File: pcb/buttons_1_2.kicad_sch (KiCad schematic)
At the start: 38 parts

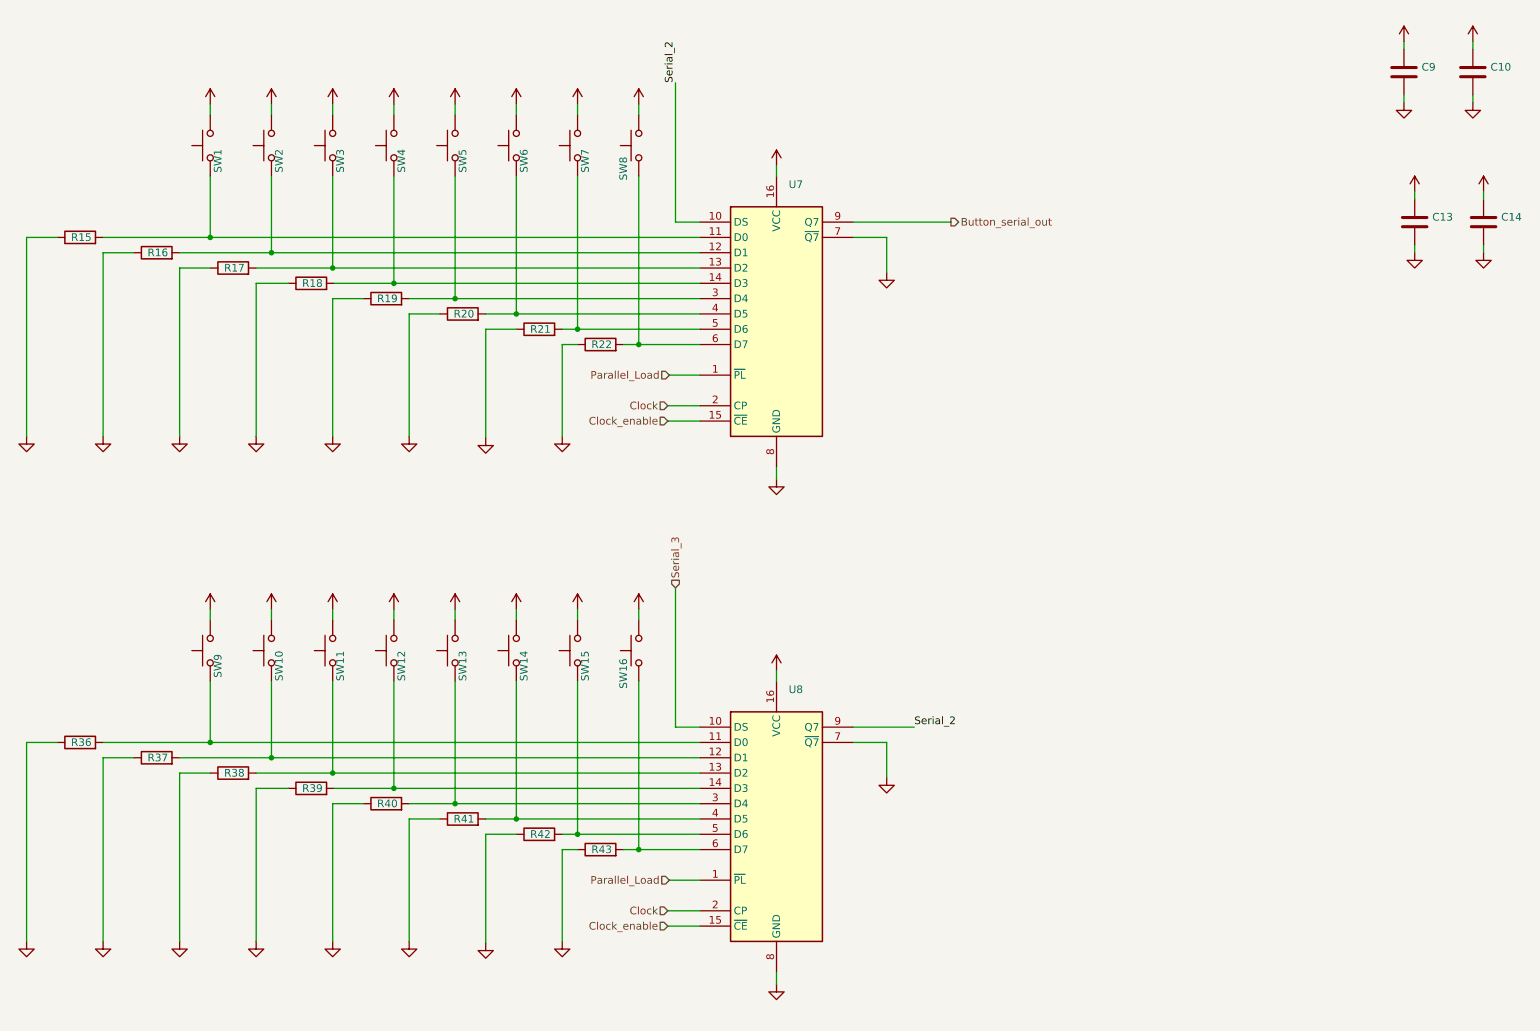
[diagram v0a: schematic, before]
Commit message: reassigned designators and layout progress
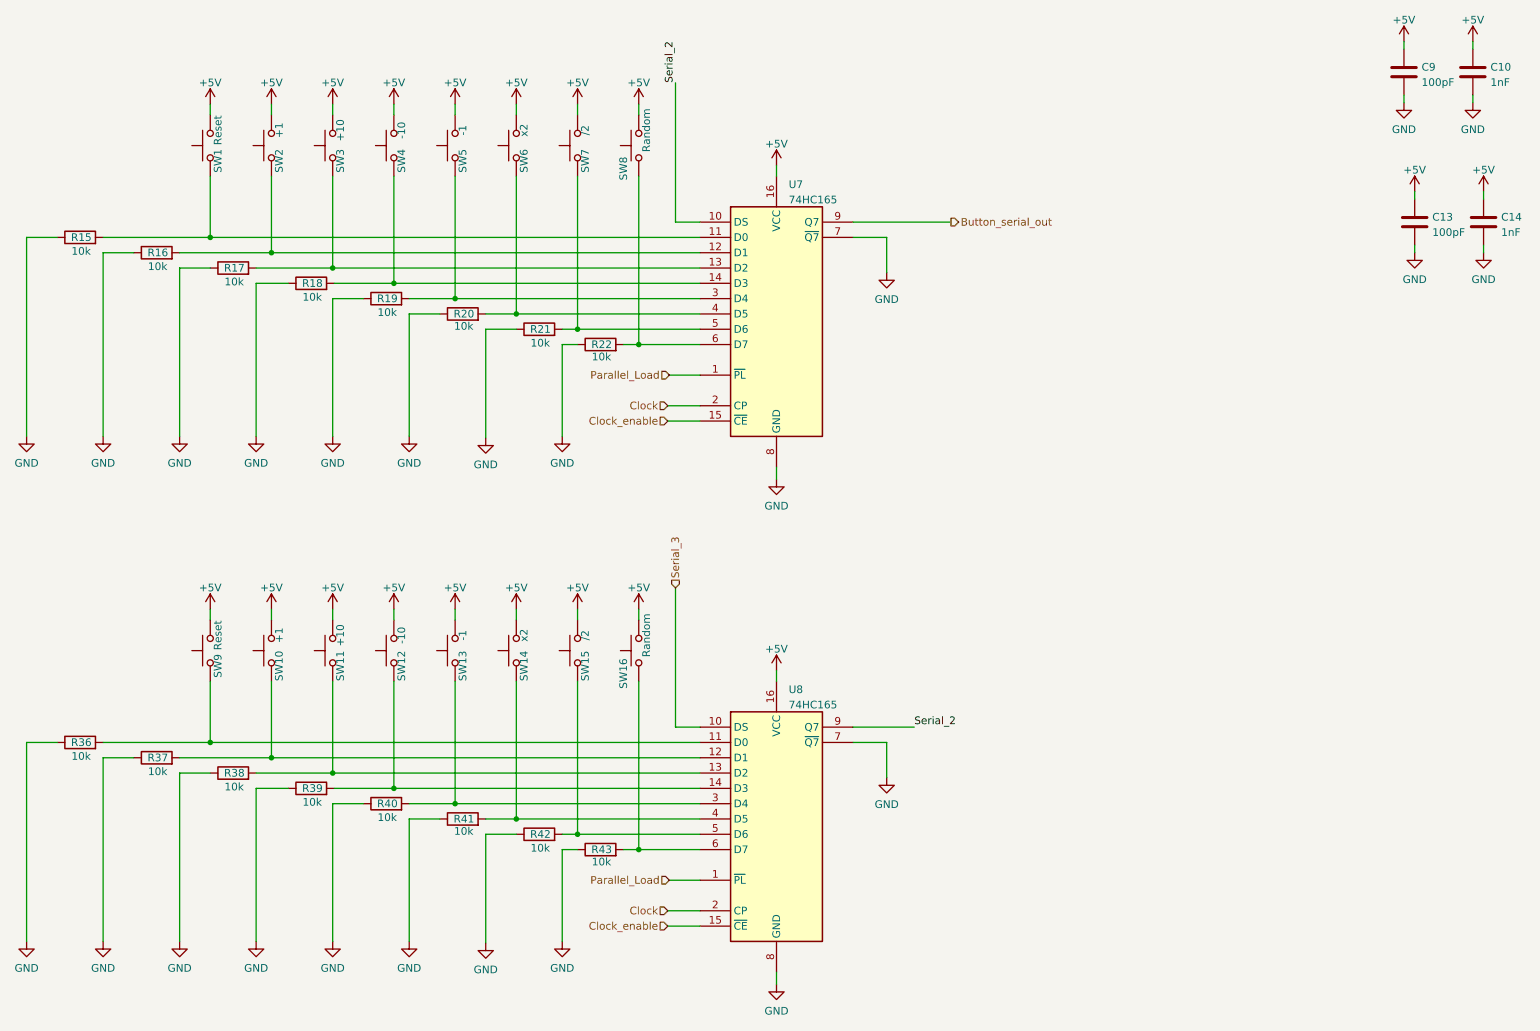
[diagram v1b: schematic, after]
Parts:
- C10, C14: value (none) -> 1nF; footprint (none) -> Capacitor_THT:C_Disc_D3.8mm_W2.6mm_P2.50mm
- C13, C9: value (none) -> 100pF; footprint (none) -> Capacitor_THT:C_Disc_D3.8mm_W2.6mm_P2.50mm
- R15, R16, R17, R18, R19, R20, R21, R22, R36, R37, R38, R39, R40, R41, R42, R43: value (none) -> 10k; footprint (none) -> Resistor_THT:R_Axial_DIN0207_L6.3mm_D2.5mm_P7.62mm_Horizontal
- SW1, SW9: value (none) -> Reset; footprint (none) -> Button_Switch_THT:SW_PUSH_6mm_H5mm
- SW10, SW2: value (none) -> +1; footprint (none) -> Button_Switch_THT:SW_PUSH_6mm_H5mm
- SW11, SW3: value (none) -> +10; footprint (none) -> Button_Switch_THT:SW_PUSH_6mm_H5mm
- SW12, SW4: value (none) -> -10; footprint (none) -> Button_Switch_THT:SW_PUSH_6mm_H5mm
- SW13, SW5: value (none) -> -1; footprint (none) -> Button_Switch_THT:SW_PUSH_6mm_H5mm
- SW14, SW6: value (none) -> x2; footprint (none) -> Button_Switch_THT:SW_PUSH_6mm_H5mm
- SW15, SW7: value (none) -> /2; footprint (none) -> Button_Switch_THT:SW_PUSH_6mm_H5mm
- SW16, SW8: value (none) -> Random; footprint (none) -> Button_Switch_THT:SW_PUSH_6mm_H5mm
- U7, U8: value (none) -> 74HC165; footprint (none) -> Package_DIP:DIP-16_W7.62mm_LongPads

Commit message: fewer parts and reduced to prototyping board with more logic analyzer pins
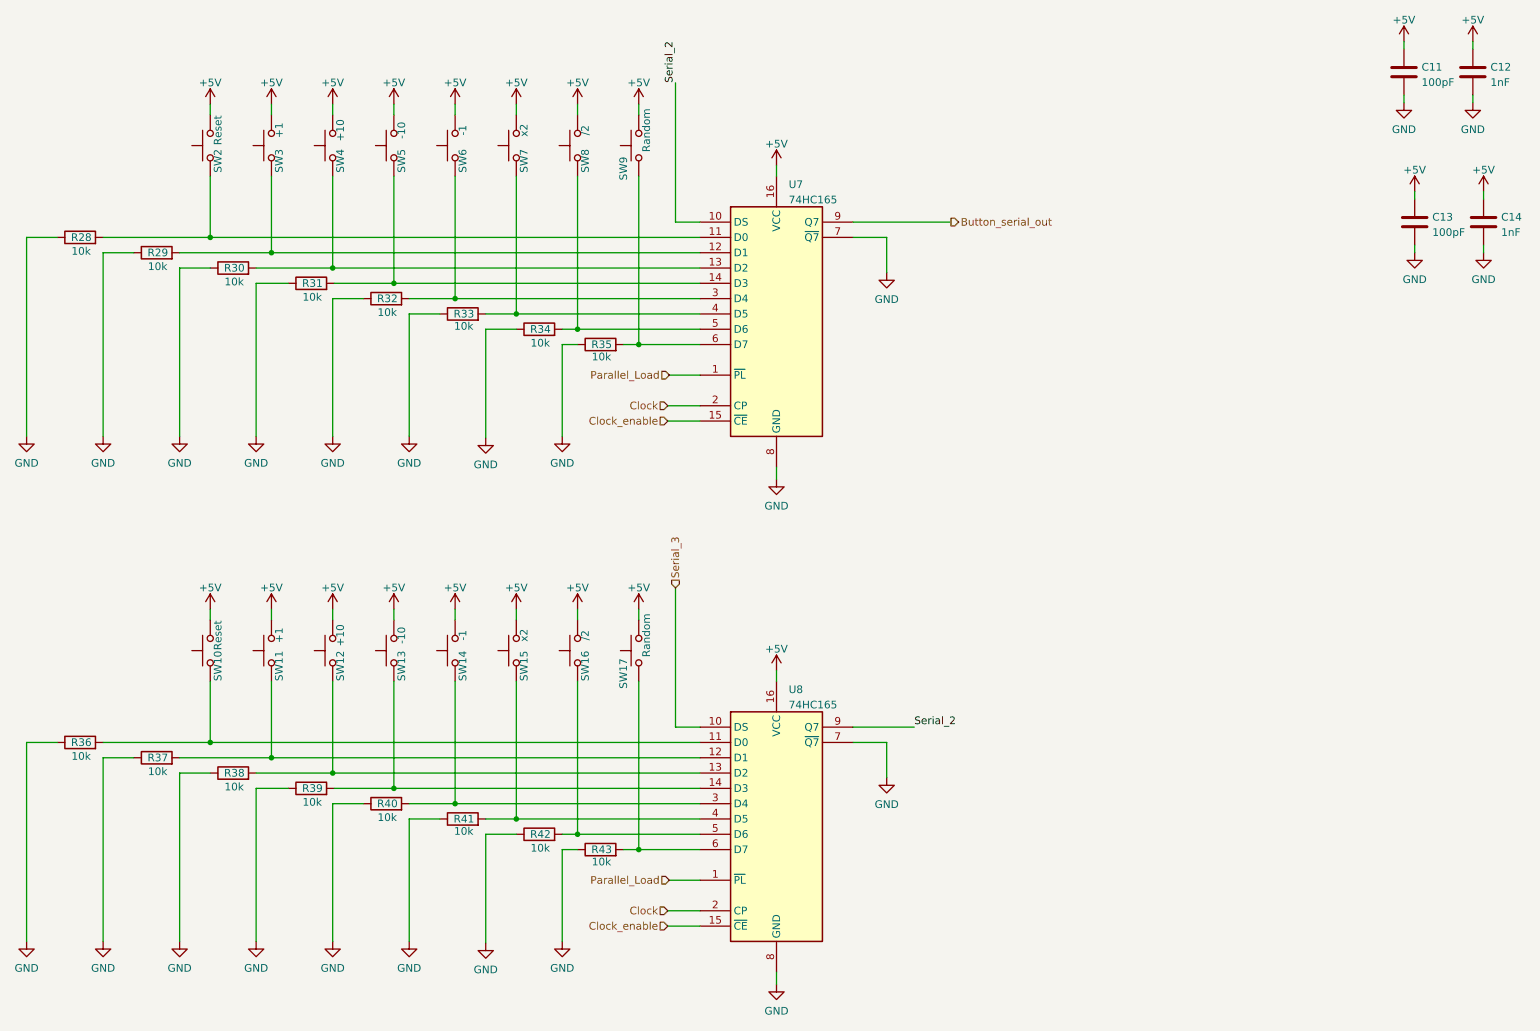
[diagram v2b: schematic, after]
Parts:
- renumbered C9 to C11, C10 to C12, R15 to R28, R16 to R29, R17 to R30, R18 to R31, R19 to R32, R20 to R33, R21 to R34, R22 to R35, SW9 to SW10, SW10 to SW11, SW11 to SW12, SW12 to SW13, SW13 to SW14, SW14 to SW15, SW15 to SW16, SW16 to SW17, SW1 to SW2, SW2 to SW3, SW3 to SW4, SW4 to SW5, SW5 to SW6, SW6 to SW7, SW7 to SW8, SW8 to SW9

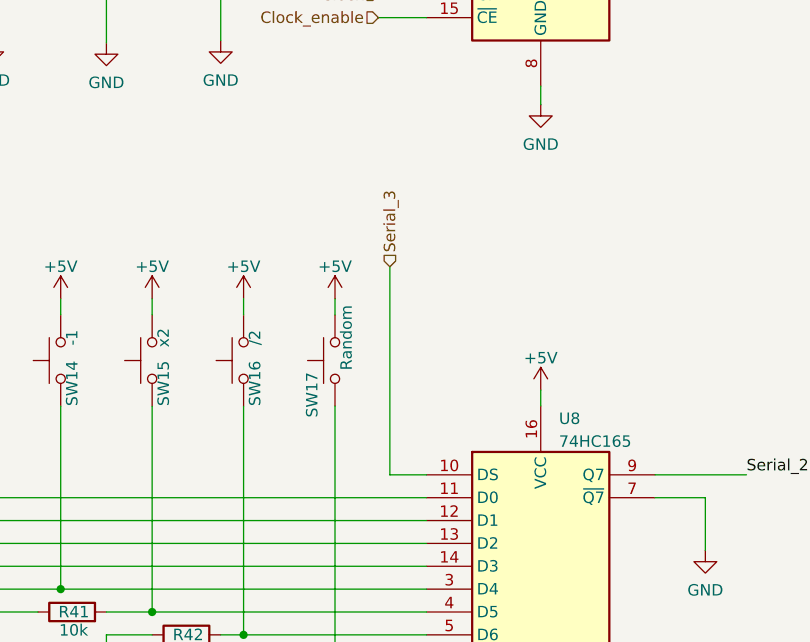
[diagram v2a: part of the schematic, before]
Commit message: reduced to 2 displays and logig analyzer output added
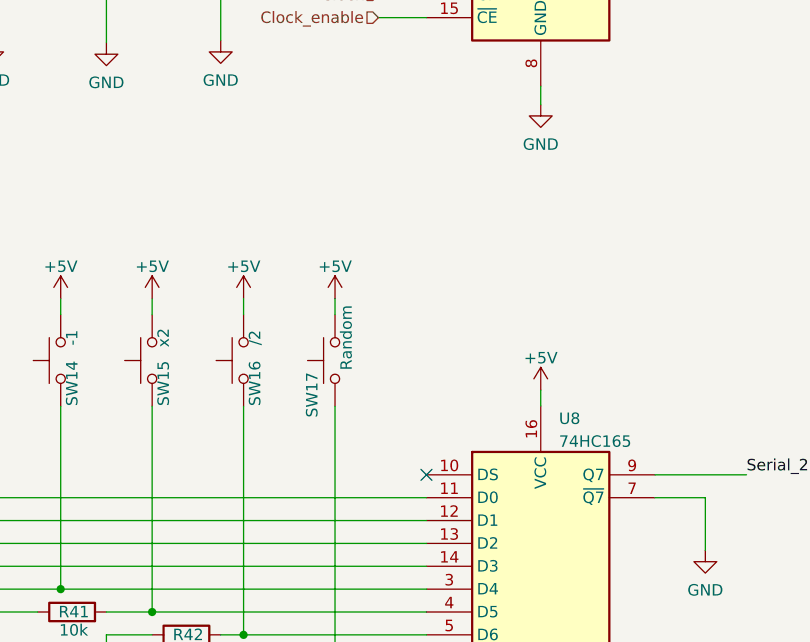
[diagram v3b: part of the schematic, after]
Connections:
- net Serial_3: no longer names the net of U8.10 (DS)
- no-connect marks 0 -> 1
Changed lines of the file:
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@@
   (junction (at 99.06 60.96) (diameter 0) (color 0 0 0 0)
   )
+  (no_connect (at 139.7 132.08))
   (wire (pts (xy 152.4 88.9) (xy 152.4 90.932))
     (stroke (width 0) (type default) (color 0 0 0 0))
@@
     (stroke (width 0) (type default) (color 0 0 0 0))
   )
-  (wire (pts (xy 135.636 108.966) (xy 135.636 132.08))
-    (stroke (width 0) (type default) (color 0 0 0 0))
-  )
   (wire (pts (xy 53.34 139.7) (xy 53.34 167.64))
     (stroke (width 0) (type default) (color 0 0 0 0))
@@
   )
   (wire (pts (xy 66.04 58.42) (xy 66.04 83.82))
-    (stroke (width 0) (type default) (color 0 0 0 0))
-  )
-  (wire (pts (xy 139.7 132.08) (xy 135.636 132.08))
     (stroke (width 0) (type default) (color 0 0 0 0))
   )
@@
     (effects (font (size 1.27 1.27)) (justify right))
   )
-  (hierarchical_label "Serial_3" (shape input) (at 135.636 108.966 90)
-    (effects (font (size 1.27 1.27)) (justify left))
-  )
   (hierarchical_label "Parallel_Load" (shape input) (at 134.62 73.66 180)

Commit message: new parts and stuff
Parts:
- added J12: Conn_01x07_Male, Connector_PinHeader_2.54mm:PinHeader_1x07_P2.54mm_Vertical, symbol Connector:Conn_01x07_Male
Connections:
- net +5V: now also J12.7 (Pin_7)
- net Button_serial_out: now also J12.6 (Pin_6)
- net Clock: now also J12.4 (Pin_4)
- net Clock_enable: now also J12.3 (Pin_3)
- net GND: now also J12.1 (Pin_1)
- net Parallel_Load: now also J12.5 (Pin_5)
- net Serial_2: now also J12.2 (Pin_2)
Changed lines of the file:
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@@
   )
   (no_connect (at 139.7 132.08))
+  (wire (pts (xy 218.44 124.46) (xy 238.76 124.46))
+    (stroke (width 0) (type default) (color 0 0 0 0))
+  )
   (wire (pts (xy 152.4 88.9) (xy 152.4 90.932))
     (stroke (width 0) (type default) (color 0 0 0 0))
@@
     (stroke (width 0) (type default) (color 0 0 0 0))
   )
+  (wire (pts (xy 218.44 115.062) (xy 218.44 116.84))
+    (stroke (width 0) (type default) (color 0 0 0 0))
+  )
   (wire (pts (xy 96.52 147.32) (xy 91.44 147.32))
     (stroke (width 0) (type default) (color 0 0 0 0))
@@
     (stroke (width 0) (type default) (color 0 0 0 0))
   )
+  (wire (pts (xy 218.44 132.08) (xy 218.44 134.112))
+    (stroke (width 0) (type default) (color 0 0 0 0))
+  )
+  (wire (pts (xy 218.44 119.38) (xy 238.76 119.38))
+    (stroke (width 0) (type default) (color 0 0 0 0))
+  )
   (wire (pts (xy 134.366 165.1) (xy 139.7 165.1))
     (stroke (width 0) (type default) (color 0 0 0 0))
   )
+  (wire (pts (xy 218.44 129.54) (xy 238.76 129.54))
+    (stroke (width 0) (type default) (color 0 0 0 0))
+  )
   (wire (pts (xy 129.54 124.46) (xy 129.54 152.4))
     (stroke (width 0) (type default) (color 0 0 0 0))
@@
     (stroke (width 0) (type default) (color 0 0 0 0))
   )
+  (wire (pts (xy 218.44 121.92) (xy 238.76 121.92))
+    (stroke (width 0) (type default) (color 0 0 0 0))
+  )
   (wire (pts (xy 78.74 60.96) (xy 83.82 60.96))
     (stroke (width 0) (type default) (color 0 0 0 0))
@@
     (stroke (width 0) (type default) (color 0 0 0 0))
   )
+  (wire (pts (xy 218.44 127) (xy 238.76 127))
+    (stroke (width 0) (type default) (color 0 0 0 0))
+  )
   (wire (pts (xy 88.9 40.64) (xy 88.9 58.42))
     (stroke (width 0) (type default) (color 0 0 0 0))
@@
   )
   (wire (pts (xy 170.688 134.62) (xy 170.688 140.462))
+    (stroke (width 0) (type default) (color 0 0 0 0))
+  )
+  (wire (pts (xy 218.44 116.84) (xy 238.76 116.84))
+    (stroke (width 0) (type default) (color 0 0 0 0))
+  )
+  (wire (pts (xy 218.44 132.08) (xy 238.76 132.08))
     (stroke (width 0) (type default) (color 0 0 0 0))
   )
@@
     (effects (font (size 1.27 1.27)) (justify left bottom))
   )
+  (label "Serial_2" (at 218.44 129.54 0)
+    (effects (font (size 1.27 1.27)) (justify left bottom))
+  )
   (hierarchical_label "Parallel_Load" (shape input) (at 134.62 157.48 180)
     (effects (font (size 1.27 1.27)) (justify right))
@@
     (effects (font (size 1.27 1.27)) (justify right))
   )
+  (hierarchical_label "Parallel_Load" (shape input) (at 218.44 121.92 180)
+    (effects (font (size 1.27 1.27)) (justify right))
+  )
   (hierarchical_label "Clock" (shape input) (at 134.366 78.74 180)
     (effects (font (size 1.27 1.27)) (justify right))
@@
   )
   (hierarchical_label "Clock" (shape input) (at 134.366 162.56 180)
+    (effects (font (size 1.27 1.27)) (justify right))
+  )
+  (hierarchical_label "Clock" (shape input) (at 218.44 124.46 180)
+    (effects (font (size 1.27 1.27)) (justify right))
+  )
+  (hierarchical_label "Button_serial_out" (shape output) (at 218.44 119.38 180)
+    (effects (font (size 1.27 1.27)) (justify right))
+  )
+  (hierarchical_label "Clock_enable" (shape input) (at 218.44 127 180)
     (effects (font (size 1.27 1.27)) (justify right))
   )
@@
     (pin "2")
   )
+  (symbol (lib_id "power:+5V") (at 218.44 115.062 0) (unit 1)
+    (in_bom yes) (on_board yes) (fields_autoplaced)
+    (property "Reference" "#PWR066" (id 0) (at 218.44 118.872 0)
+      (effects (font (size 1.27 1.27)) hide)
+    )
+    (property "Value" "+5V" (id 1) (at 218.44 111.4862 0))
+    (property "Footprint" "" (id 2) (at 218.44 115.062 0)
+      (effects (font (size 1.27 1.27)) hide)
+    )
+    (property "Datasheet" "" (id 3) (at 218.44 115.062 0)
+      (effects (font (size 1.27 1.27)) hide)
+    )
+    (pin "1")
+  )
   (symbol (lib_id "power:GND") (at 152.4 174.752 0) (unit 1)
     (in_bom yes) (on_board yes) (fields_autoplaced)
@@
     (pin "1")
   )
+  (symbol (lib_id "power:GND") (at 218.44 134.112 0) (unit 1)
+    (in_bom yes) (on_board yes) (fields_autoplaced)
+    (property "Reference" "#PWR067" (id 0) (at 218.44 140.462 0)
+      (effects (font (size 1.27 1.27)) hide)
+    )
+    (property "Value" "GND" (id 1) (at 218.44 138.5554 0))
+    (property "Footprint" "" (id 2) (at 218.44 134.112 0)
+      (effects (font (size 1.27 1.27)) hide)
+    )
+    (property "Datasheet" "" (id 3) (at 218.44 134.112 0)
+      (effects (font (size 1.27 1.27)) hide)
+    )
+    (pin "1")
+  )
   (symbol (lib_id "power:+5V") (at 78.74 112.522 0) (unit 1)
     (in_bom yes) (on_board yes) (fields_autoplaced)
@@
     (pin "2")
   )
+  (symbol (lib_id "Connector:Conn_01x07_Male") (at 243.84 124.46 180) (unit 1)
+    (in_bom yes) (on_board yes) (fields_autoplaced)
+    (property "Reference" "J12" (id 0) (at 244.5512 123.6253 0)
+      (effects (font (size 1.27 1.27)) (justify right))
+    )
+    (property "Value" "Conn_01x07_Male" (id 1) (at 244.5512 126.1622 0)
+      (effects (font (size 1.27 1.27)) (justify right))
+    )
+    (property "Footprint" "Connector_PinHeader_2.54mm:PinHeader_1x07_P2.54mm_Vertical" (id 2) (at 243.84 124.46 0)
+      (effects (font (size 1.27 1.27)) hide)
+    )
+    (property "Datasheet" "~" (id 3) (at 243.84 124.46 0)
+      (effects (font (size 1.27 1.27)) hide)
+    )
+    (pin "1")
+    (pin "2")
+    (pin "3")
+    (pin "4")
+    (pin "5")
+    (pin "6")
+    (pin "7")
+  )
   (symbol (lib_id "power:GND") (at 53.34 83.82 0) (unit 1)

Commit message: layout changes
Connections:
- net Button_serial_out: now also J12.3 (Pin_3); no longer J12.6 (Pin_6)
- net Clock: now also J12.6 (Pin_6); no longer J12.4 (Pin_4)
- net Clock_enable: now also J12.4 (Pin_4); no longer J12.3 (Pin_3)
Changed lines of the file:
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@@
     (effects (font (size 1.27 1.27)) (justify right))
   )
-  (hierarchical_label "Clock" (shape input) (at 218.44 124.46 180)
+  (hierarchical_label "Clock" (shape input) (at 218.44 119.38 180)
     (effects (font (size 1.27 1.27)) (justify right))
   )
-  (hierarchical_label "Button_serial_out" (shape output) (at 218.44 119.38 180)
+  (hierarchical_label "Button_serial_out" (shape output) (at 218.44 127 180)
     (effects (font (size 1.27 1.27)) (justify right))
   )
-  (hierarchical_label "Clock_enable" (shape input) (at 218.44 127 180)
+  (hierarchical_label "Clock_enable" (shape input) (at 218.44 124.46 180)
     (effects (font (size 1.27 1.27)) (justify right))
   )
